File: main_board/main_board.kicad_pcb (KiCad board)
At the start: 4 copper layers, 85 x 55 mm, 56 parts, among them J1 USB4105-GF-A-060, J2 Conn_ARM_JTAG_SWD_10, Q3 NX3008PBK,215, U1 SSD1306, U2 ESP32-S2-SOLO, U3 TLV62568PDRLT, U4 MCP73832, U5 DW01, U6 8205A, U7 MAX17055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

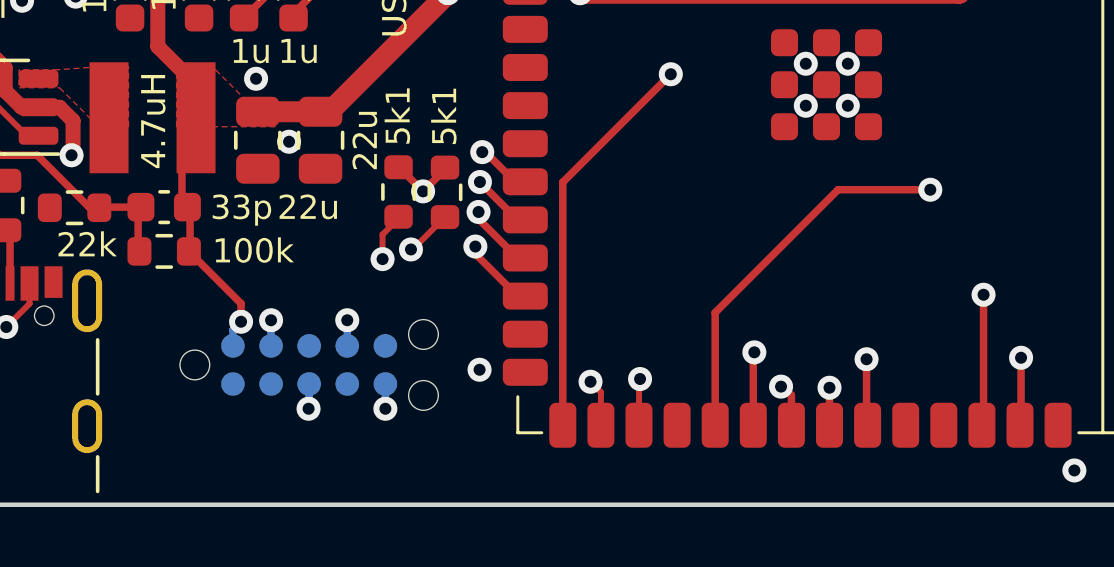
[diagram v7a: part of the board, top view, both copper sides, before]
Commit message: Remove JTAG port
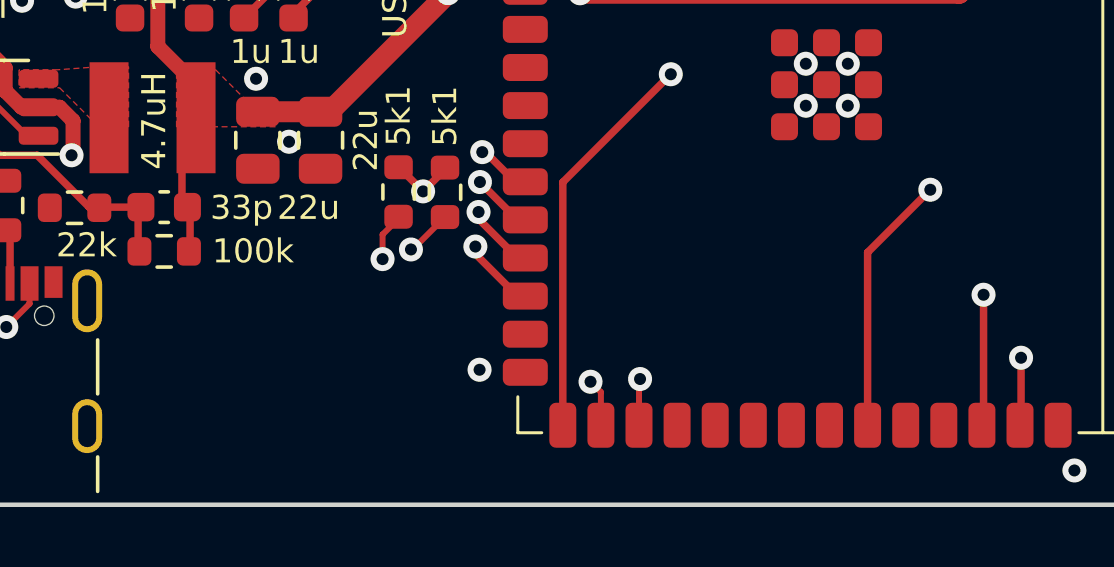
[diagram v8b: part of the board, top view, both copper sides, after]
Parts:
- removed J2: Conn_ARM_JTAG_SWD_10, Connector:Tag-Connect_TC2050-IDC-NL_2x05_P1.27mm_Vertical
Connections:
- U2 pad 31: /ECG_CLK_EN -> unconnected-(U2-IO38-Pad31)
- U2 pad 32: Net-(J2-SWDCLK/TCK) -> unconnected-(U2-IO39-Pad32)
- U2 pad 33: Net-(J2-SWO/TDO) -> unconnected-(U2-IO40-Pad33)
- U2 pad 34: Net-(J2-NC/TDI) -> unconnected-(U2-IO41-Pad34)
- U2 pad 35: Net-(J2-SWDIO/TMS) -> /ECG_CLK_EN
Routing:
- net Net-(J2-SWDIO/TMS): track 23.8 -> 0.00 mm, vias 2 -> 0
- net Net-(J2-NC/TDI): track 20.1 -> 0.00 mm, vias 2 -> 0
- net Net-(J2-SWDCLK/TCK): track 17.6 -> 0.00 mm, vias 2 -> 0
- net Net-(J2-SWO/TDO): track 16.1 -> 0.00 mm, vias 2 -> 0
- net /ECG_CLK_EN: track 48.2 -> 43.8 mm
- net +3V3: track 60.8 -> 56.8 mm, vias 3 -> 2
